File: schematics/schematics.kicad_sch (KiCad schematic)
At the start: 27 parts, among them SW1 RESET, U1 STM32F103VBT6, U2 AMS1117-3.3, Y1 16Mhz

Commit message: Configure ignored files
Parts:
- added C12: 100nF, Capacitor_SMD:C_0603_1608Metric, symbol Device:C
- FB1: value FerriteBead -> 100R @ 100Mhz
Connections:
- net +3.3V: now also C12.1
- net GND: now also C12.2
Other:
- note added: "Fuse 100mA min"
- moved on the sheet: C1, C2, D1, R2, U2

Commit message: Update the board schematics
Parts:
- removed C5: 100nF, Capacitor_SMD:C_0603_1608Metric, symbol Device:C
- removed FB1: 100R @ 100Mhz, Inductor_SMD:L_0603_1608Metric, symbol Device:FerriteBead
- removed R3: 10k, Resistor_SMD:R_0603_1608Metric, symbol Device:R
- removed SW1: RESET, Custom:SW_Push_SMD_4x4x1.5, symbol Switch:SW_Push
- added J3: 2K, Custom:RPP_48G2_3T3_Male, symbol Connector_Generic:Conn_02x24_Odd_Even
- added J4: POWER, Connector_JST:JST_EH_B2B-EH-A_1x02_P2.50mm_Vertical, symbol Connector:Conn_01x02_Pin
- renumbered C3 to C1, C11 to C10, C12 to C11, C1 to C2, C4 to C3, C9 to C4, C10 to C5, C2 to C7, C7 to C8, C8 to C9, R5 to R2, R2 to R3, R6 to R4, R7 to R5, R8 to R6
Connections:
- net PWR is gone; now on net VBUS: C2.1, U2.3 (VI)
- net GND: now also J4.2 (Pin_2)
- net OSC_OUT: no longer C4.1, R2.1, Y1.3
- net VBUS: now also J4.1 (Pin_1)
- net Data_Bus_Input_04: now reaches U1.1 (PE2)
- net Data_Bus_Input_04: now also J3.5 (Pin_5)
- net Data_Bus_Input_06: now reaches U1.2 (PE3)
- net Data_Bus_Input_06: now also J3.6 (Pin_6)
- net Data_Bus_Input_05: now reaches U1.3 (PE4)
- net Data_Bus_Input_05: now also J3.3 (Pin_3)
- net Data_Bus_Input_07: now reaches U1.4 (PE5)
- net Data_Bus_Input_07: now also J3.4 (Pin_4)
- net Data_Transfer_Short_Input: now reaches U1.48 (PB11)
- net Data_Transfer_Short_Input: now also J3.14 (Pin_14)
- net External_Set_Output: now reaches U1.5 (PE6)
- net External_Set_Output: now also J3.1 (Pin_1)
- net External_Reset_Output: now reaches U1.51 (PB12)
- net External_Reset_Output: now also J3.47 (Pin_47)
- net Data_Transfer_Long_Input: now reaches U1.52 (PB13)
- net Data_Transfer_Long_Input: now also J3.45 (Pin_45)
- net Data_Transfer_Completed_Input: now reaches U1.53 (PB14)
- net Data_Transfer_Completed_Input: now also J3.46 (Pin_46)
- net Data_Bus_Output_14: now reaches U1.54 (PB15)
- net Data_Bus_Output_14: now also J3.43 (Pin_43)
- net Data_Bus_Output_11: now reaches U1.55 (PD8)
- net Data_Bus_Output_11: now also J3.44 (Pin_44)
- net Data_Bus_Output_15: now reaches U1.56 (PD9)
- net Data_Bus_Output_15: now also J3.41 (Pin_41)
- net Ready_Output: now reaches U1.57 (PD10)
- net Ready_Output: now also J3.42 (Pin_42)
- net Data_Bus_Output_12: now reaches U1.58 (PD11)
- net Data_Bus_Output_12: now also J3.39 (Pin_39)
- net Data_Bus_Output_13: now reaches U1.59 (PD12)
- net Data_Bus_Output_13: now also J3.40 (Pin_40)
- net Data_Bus_Output_10: now reaches U1.60 (PD13)
- net Data_Bus_Output_10: now also J3.37 (Pin_37)
- net Data_Bus_Output_08: now reaches U1.61 (PD14)
- net Data_Bus_Output_08: now also J3.38 (Pin_38)
- net Data_Bus_Output_07: now reaches U1.62 (PD15)
- net Data_Bus_Output_07: now also J3.35 (Pin_35)
- net Data_Bus_Output_09: now reaches U1.63 (PC6)
- net Data_Bus_Output_09: now also J3.36 (Pin_36)
- net Data_Bus_Output_06: now reaches U1.64 (PC7)
- net Data_Bus_Output_06: now also J3.33 (Pin_33)
- net Data_Bus_Output_05: now reaches U1.65 (PC8)
- net Data_Bus_Output_05: now also J3.34 (Pin_34)
- net Data_Bus_Output_04: now reaches U1.66 (PC9)
- net Data_Bus_Output_04: now also J3.31 (Pin_31)
- net Data_Bus_Output_03: now reaches U1.67 (PA8)
- net Data_Bus_Output_03: now also J3.32 (Pin_32)
- net Data_Bus_Output_Control_1: now reaches U1.68 (PA9)
- net Data_Bus_Output_Control_1: now also J3.29 (Pin_29)
- net Data_Bus_Output_02: now reaches U1.69 (PA10)
- net Data_Bus_Output_02: now also J3.30 (Pin_30)
- net Data_Bus_Output_Control_0: now reaches U1.70 (PA11)
- net Data_Bus_Output_Control_0: now also J3.27 (Pin_27)
- net Data_Bus_Output_01: now reaches U1.71 (PA12)
- net Data_Bus_Output_01: now also J3.28 (Pin_28)
- net Internal_Error_Output: now reaches U1.77 (PA15)
- net Internal_Error_Output: now also J3.25 (Pin_25)
- net Data_Bus_Output_00: now reaches U1.78 (PC10)
- net Data_Bus_Output_00: now also J3.26 (Pin_26)
- net Data_Transfer_Completed_Output: now reaches U1.79 (PC11)
- net Data_Transfer_Completed_Output: now also J3.23 (Pin_23)
- net Data_Bus_Output_Control_State: now reaches U1.80 (PC12)
- net Data_Bus_Output_Control_State: now also J3.24 (Pin_24)
- net Data_Bus_Input_15: now reaches U1.81 (PD0)
- net Data_Bus_Input_15: now also J3.21 (Pin_21)
- net Data_Bus_Input_13: now reaches U1.82 (PD1)
- net Data_Bus_Input_13: now also J3.22 (Pin_22)
- net Data_Bus_Input_Control_0: now reaches U1.83 (PD2)
- net Data_Bus_Input_Control_0: now also J3.19 (Pin_19)
- net Data_Bus_Input_14: now reaches U1.84 (PD3)
- net Data_Bus_Input_14: now also J3.20 (Pin_20)
- net Data_Bus_Input_12: now reaches U1.85 (PD4)
- net Data_Bus_Input_12: now also J3.17 (Pin_17)
- net Data_Bus_Input_10: now reaches U1.86 (PD5)
- net Data_Bus_Input_10: now also J3.18 (Pin_18)
- net Data_Bus_Input_09: now reaches U1.87 (PD6)
- net Data_Bus_Input_09: now also J3.15 (Pin_15)
- net Data_Bus_Input_11: now reaches U1.88 (PD7)
- net Data_Bus_Input_11: now also J3.16 (Pin_16)
- net SWO: now reaches U1.89 (PB3)
- net Data_Bus_Input_08: now reaches U1.90 (PB4)
- net Data_Bus_Input_08: now also J3.13 (Pin_13)
- net Data_Bus_Input_00: now reaches U1.92 (PB6)
- net Data_Bus_Input_00: now also J3.11 (Pin_11)
- net Data_Bus_Input_Control_1: now reaches U1.93 (PB7)
- net Data_Bus_Input_Control_1: now also J3.12 (Pin_12)
- net Reset_Input: now reaches U1.95 (PB8)
- net Reset_Input: now also J3.9 (Pin_9)
- net Data_Bus_Input_02: now reaches U1.96 (PB9)
- net Data_Bus_Input_02: now also J3.10 (Pin_10)
- net Data_Bus_Input_01: now reaches U1.97 (PE0)
- net Data_Bus_Input_01: now also J3.7 (Pin_7)
- net Data_Bus_Input_03: now reaches U1.98 (PE1)
- net Data_Bus_Input_03: now also J3.8 (Pin_8)
- new net: C4.1, R2.1, Y1.3
- no-connect marks 70 -> 25
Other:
- note added: "2K Interface"
- note added: "5V VBUS and GND from POWER connector."
- note added: "Current consumption 50mA @ 72Mhz IO raise/fall time - 4ns IO max fequency - 30MHz EXTI detection time - 10ns"
- note added: "MCU VDD filtering"
- note added: "MCU in current design offers: - 26 available pins - 15 available 5v tolerant pins: PORT A - [8 - 12] PORT B - [2, 3], [6, 7], [10 - 15] PORT C - [8, 9]"
- note added: "Male connector - РПП-48Г2-3Т3 Target board - БИФ ИРПР/2К Not used pins 32, 24, 25"
- note added: "Place each capacitor as close as possible to the corresponding MCU power pin."
- note removed: "Fuse 100mA min"
- note removed: "MCU in current design offers: - 69 available pins - 54 available 5v tolerant pins: PORT A - [8 - 12], 15 PORT B - [2 - 4], [6 - 15] PORT C - [6 - 12] PORT D - [0 - 15] PORT E - [0 - 15]"
- note removed: "Reset"
- note removed: "VBUS from SM2M connector pins 1A, 1B and 1C. GND from SM2M connector pins 32A, 32B and 32C."
- note removed: "VDD filtering"
- moved on the sheet: C1, C10, C11, C2, C3, C4, C5, C6, C7, C8, C9, D1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

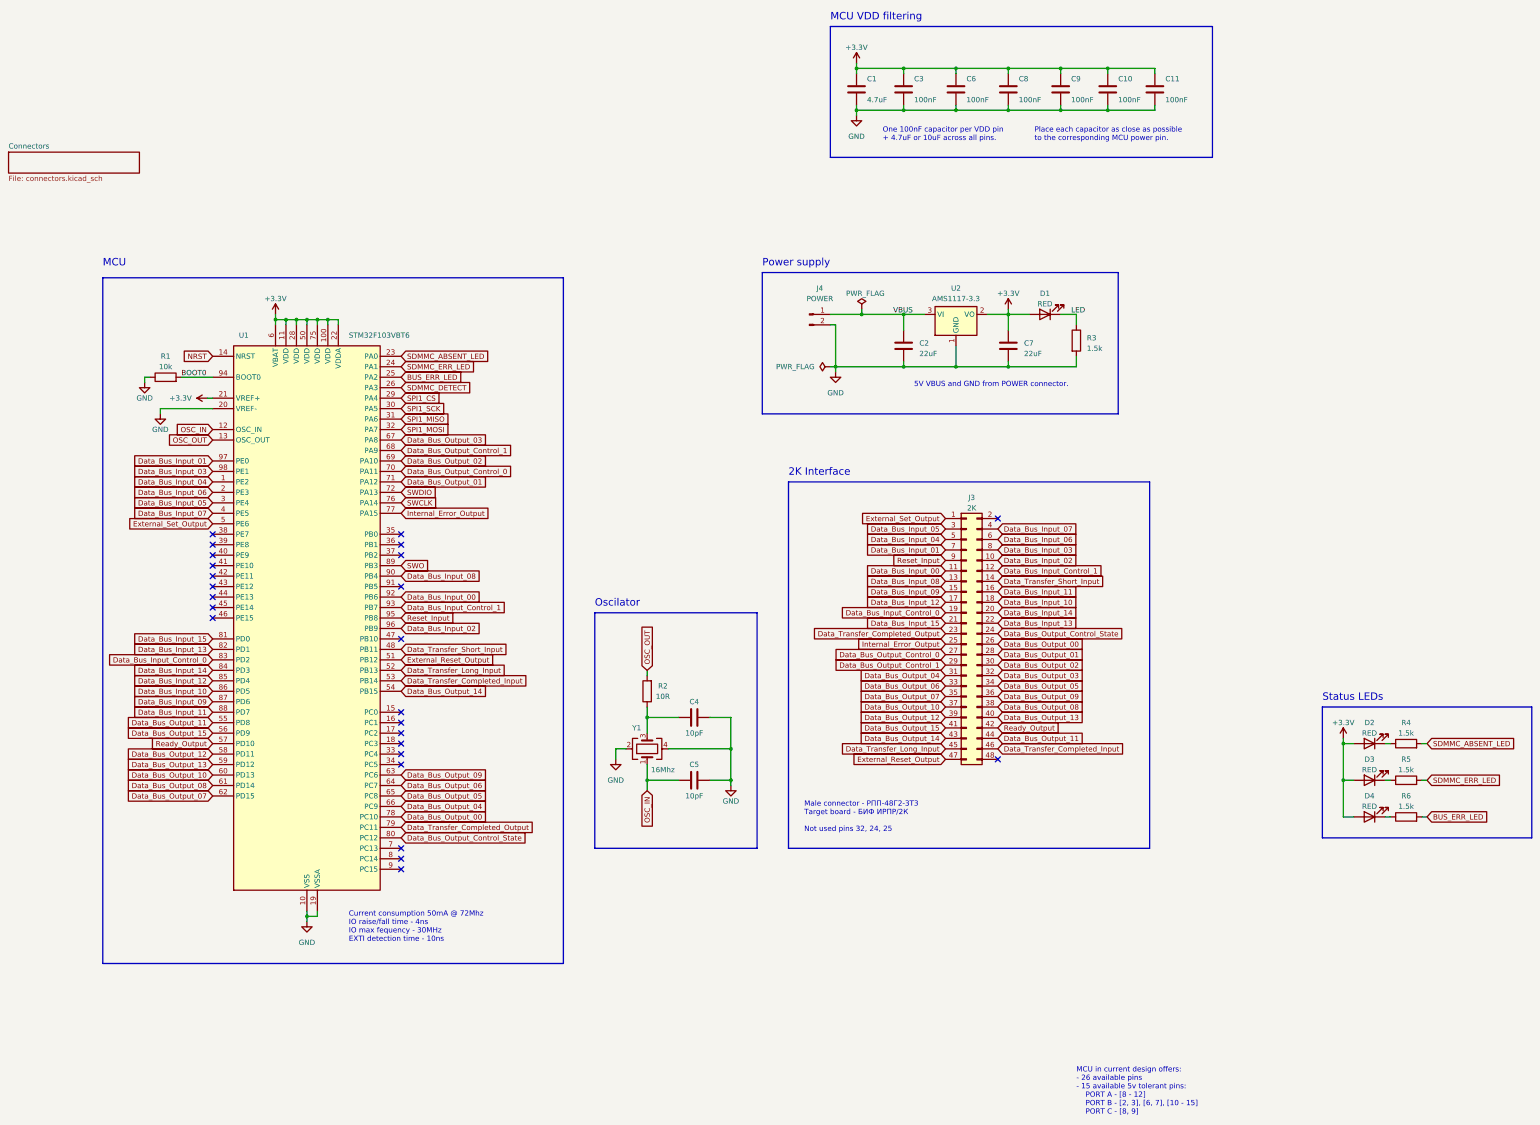
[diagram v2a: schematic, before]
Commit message: Re-route data buses and add heap allocator
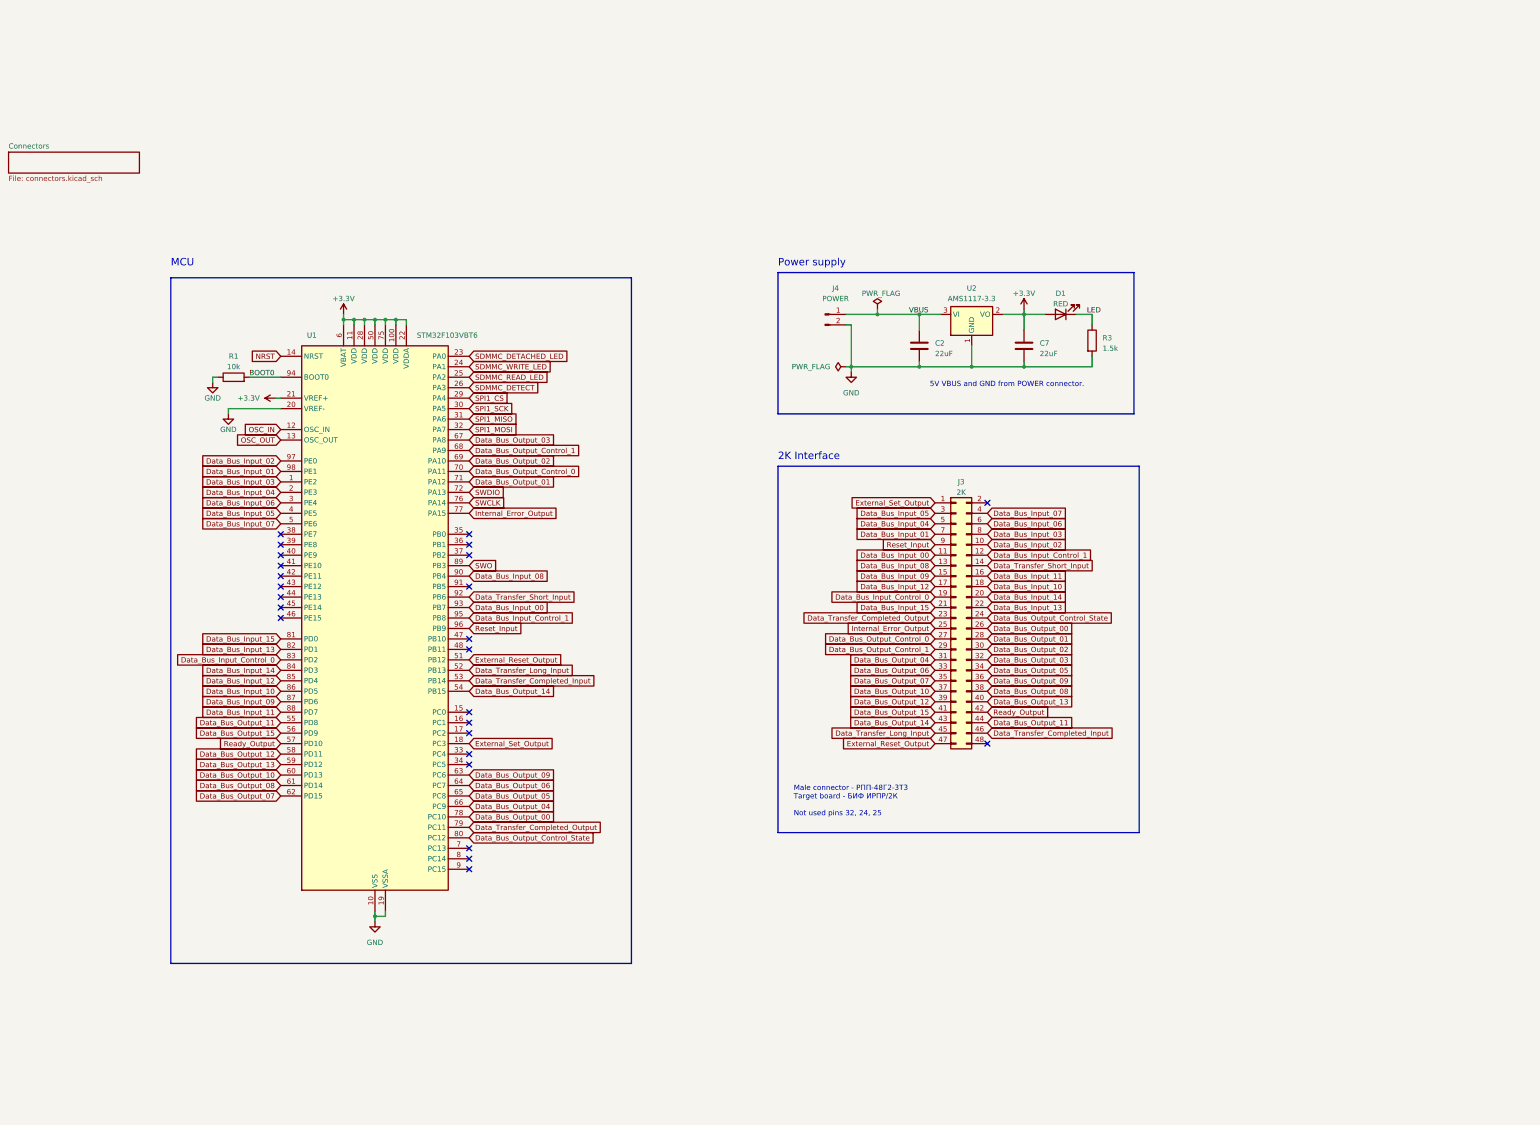
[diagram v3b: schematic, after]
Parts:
- removed C1: 4.7uF, Capacitor_SMD:C_0603_1608Metric, symbol Device:C
- removed C10, C11, C3, C6, C8, C9: 100nF, Capacitor_SMD:C_0603_1608Metric, symbol Device:C
- removed C4, C5: 10pF, Capacitor_SMD:C_0603_1608Metric, symbol Device:C
- removed D2, D3, D4: RED, LED_SMD:LED_0603_1608Metric, symbol Device:LED
- removed R2: 10R, Resistor_SMD:R_0603_1608Metric, symbol Device:R
- removed R4, R5, R6: 1.5k, Resistor_SMD:R_0603_1608Metric, symbol Device:R
- removed Y1: 16Mhz, Crystal:Crystal_SMD_3225-4Pin_3.2x2.5mm, symbol Device:Crystal_GND24
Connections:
- net Data_Bus_Input_00: now also U1.93 (PB7); no longer U1.92 (PB6)
- net Data_Bus_Input_01: now also U1.98 (PE1); no longer U1.97 (PE0)
- net Data_Bus_Input_02: now also U1.97 (PE0); no longer U1.96 (PB9)
- net Data_Bus_Input_03: now also U1.1 (PE2); no longer U1.98 (PE1)
- net Data_Bus_Input_04: now also U1.2 (PE3); no longer U1.1 (PE2)
- net Data_Bus_Input_05: now also U1.4 (PE5); no longer U1.3 (PE4)
- net Data_Bus_Input_06: now also U1.3 (PE4); no longer U1.2 (PE3)
- net Data_Bus_Input_07: now also U1.5 (PE6); no longer U1.4 (PE5)
- net Data_Bus_Input_Control_1: now also U1.95 (PB8); no longer U1.93 (PB7)
- net Data_Transfer_Short_Input: now also U1.92 (PB6); no longer U1.48 (PB11)
- net External_Set_Output: now also U1.18 (PC3); no longer U1.5 (PE6)
- net Reset_Input: now also U1.96 (PB9); no longer U1.95 (PB8)
- net BUS_ERR_LED renamed SDMMC_READ_LED
- net SDMMC_ABSENT_LED renamed SDMMC_DETACHED_LED
- net SDMMC_ERR_LED renamed SDMMC_WRITE_LED
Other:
- note removed: "Current consumption 50mA @ 72Mhz IO raise/fall time - 4ns IO max fequency - 30MHz EXTI detection time - 10ns"
- note removed: "MCU VDD filtering"
- note removed: "MCU in current design offers: - 26 available pins - 15 available 5v tolerant pins: PORT A - [8 - 12] PORT B - [2, 3], [6, 7], [10 - 15] PORT C - [8, 9]"
- note removed: "One 100nF capacitor per VDD pin + 4.7uF or 10uF across all pins."
- note removed: "Oscilator"
- note removed: "Place each capacitor as close as possible to the corresponding MCU power pin."
- note removed: "Status LEDs"
- moved on the sheet: C2, C7, D1, J3, J4, R1, R3, U1, U2
